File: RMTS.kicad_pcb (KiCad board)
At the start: 2 copper layers, 78.1 x 50.2 mm, 58 parts, among them J1 USB_B_Mini, J10 CONN_02, J2 Programmer, J3 Screw_Terminal_01x03, J4 Screw_Terminal_01x04, J5 Screw_Terminal_01x02, J6 Screw_Terminal_01x02, J7 Micro_SD_Card_Det_Hirose_DM3AT, J9 CONN_02, Q1 PMV20ENR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

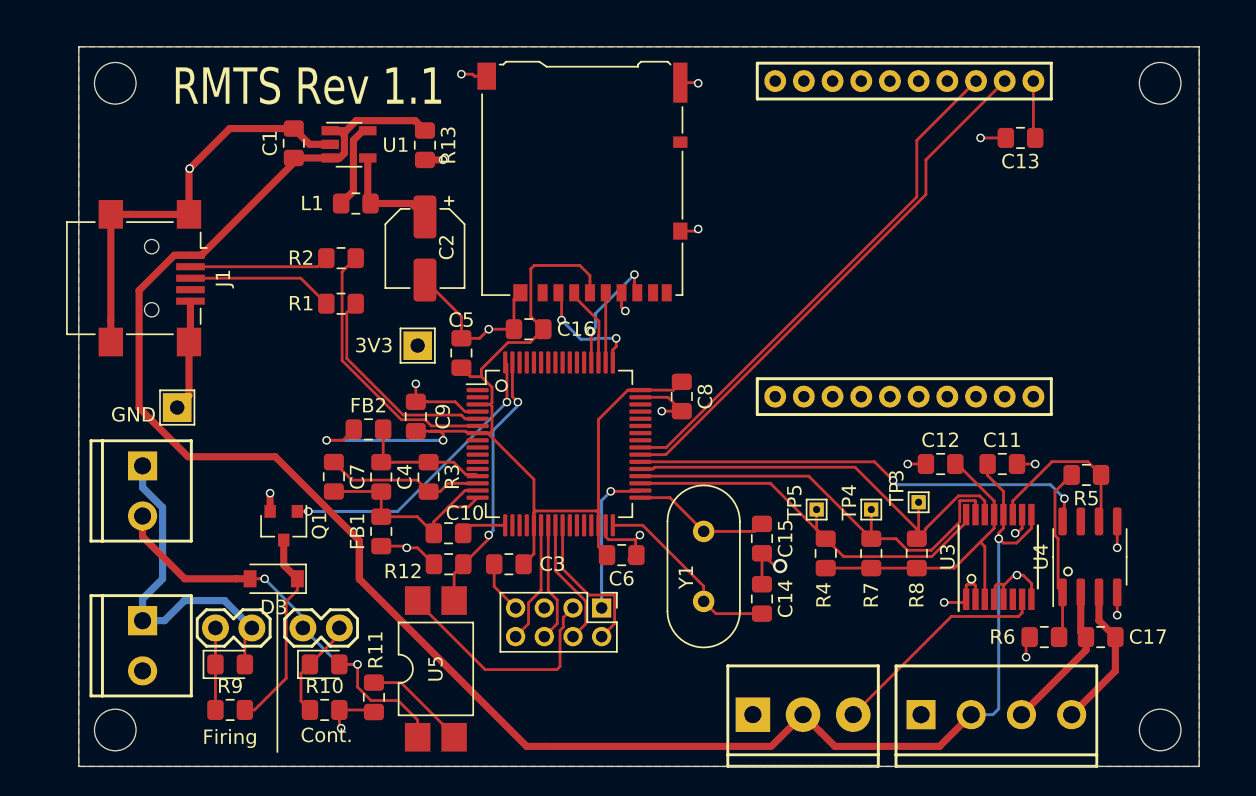
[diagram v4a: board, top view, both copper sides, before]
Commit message: Updated amplifier to MCP6N16, incremented revision number
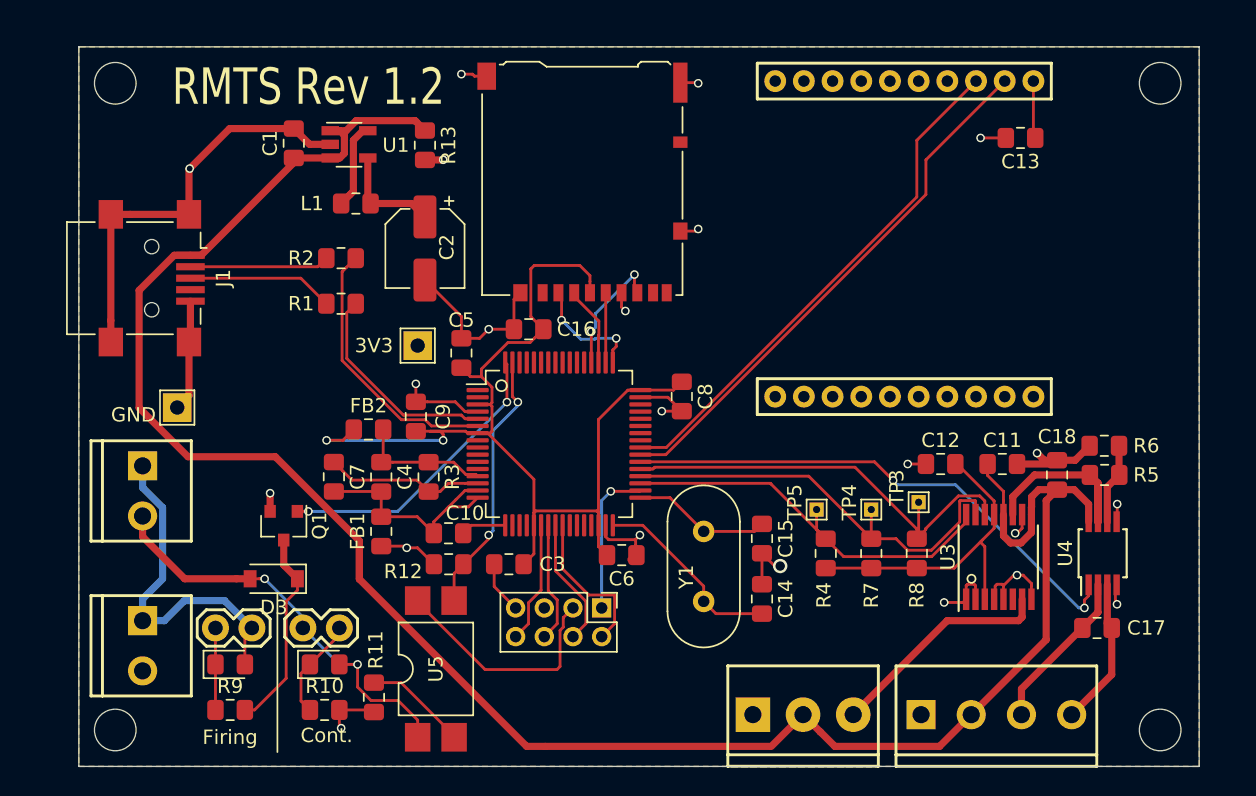
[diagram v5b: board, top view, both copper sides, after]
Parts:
- added C18: 0.1uF, Capacitor_SMD:C_0805_2012Metric_Pad1.15x1.40mm_HandSolder, F.Cu at (200.3, 92.1)
- U4: value MCP6N11 -> MCP6N16; footprint Package_SO:SOIC-8_3.9x4.9mm_P1.27mm -> Package_SO:MSOP-8_3x3mm_P0.65mm
- moved R6 14.0 mm to (203.6, 90.0)
- moved R5 1.27 mm to (203.6, 92.1), turned to 0 degrees
- moved U4 0.92 mm to (203.5, 97.5)
- moved C17 0.68 mm to (203.1, 102.7)
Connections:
- R5 pad 2: /FG0 -> Net-(R5-Pad2)
- R6 pad 1: /FG0 -> Net-(R5-Pad2)
- U4 pad 1: /FG0 -> /AMP_EN
- U4 pad 6: /LC0 -> Net-(R5-Pad2)
- U4 pad 7: +3V3 -> /LC0
- U4 pad 8: /AMP_EN -> /VBUS
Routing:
- net /FG0: track 12.1 -> 0.00 mm
- net /VBUS: track 134.4 -> 145.3 mm, vias 1 -> 0
- net Net-(R5-Pad2): track 0.00 -> 5.67 mm
- net /AMP_EN: track 32.3 -> 36.9 mm
- net GND: track 109.1 -> 113.2 mm, vias 23 -> 22
- net /LC0: track 11.9 -> 14.2 mm
- net Net-(C17-Pad2): track 10.5 -> 11.3 mm
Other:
- board text added: "RMTS Rev 1.2"
- board text removed: "RMTS Rev 1.1"

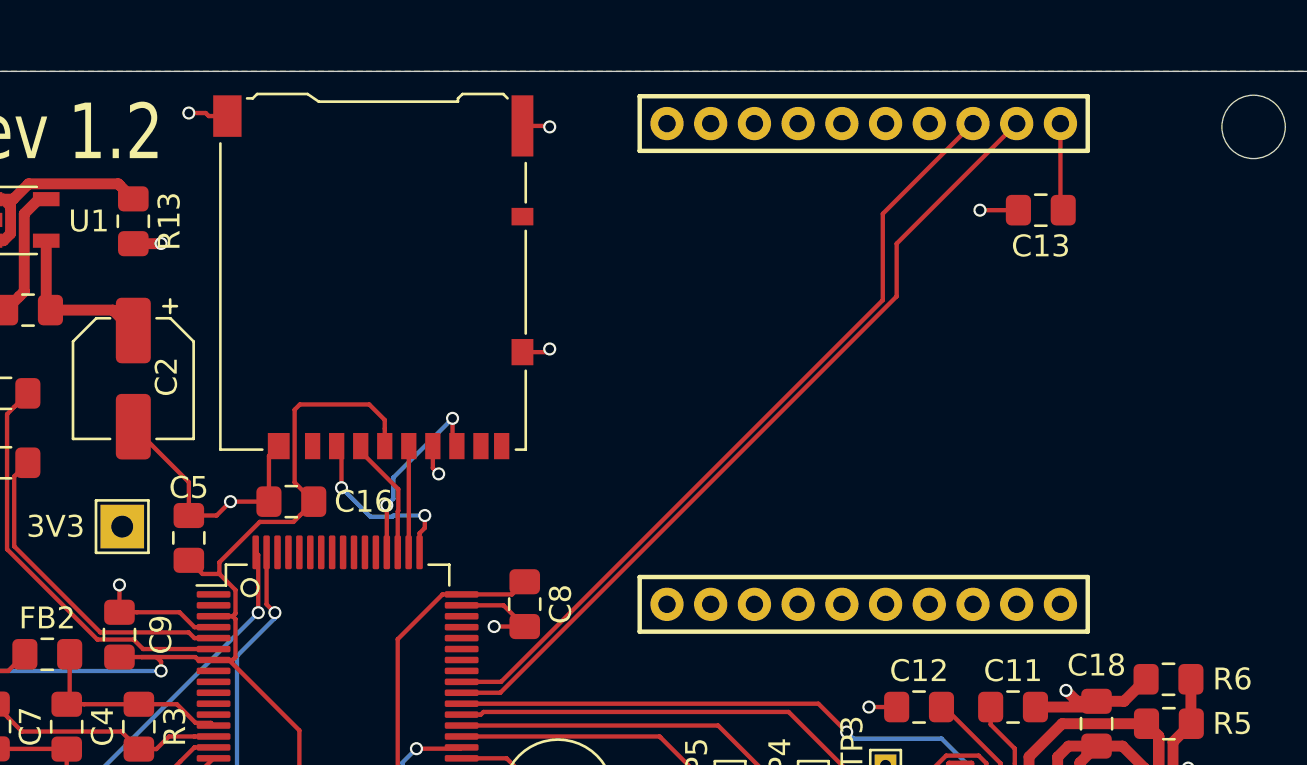
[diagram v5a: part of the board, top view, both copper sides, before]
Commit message: Flipped SD card, added external firing circuit
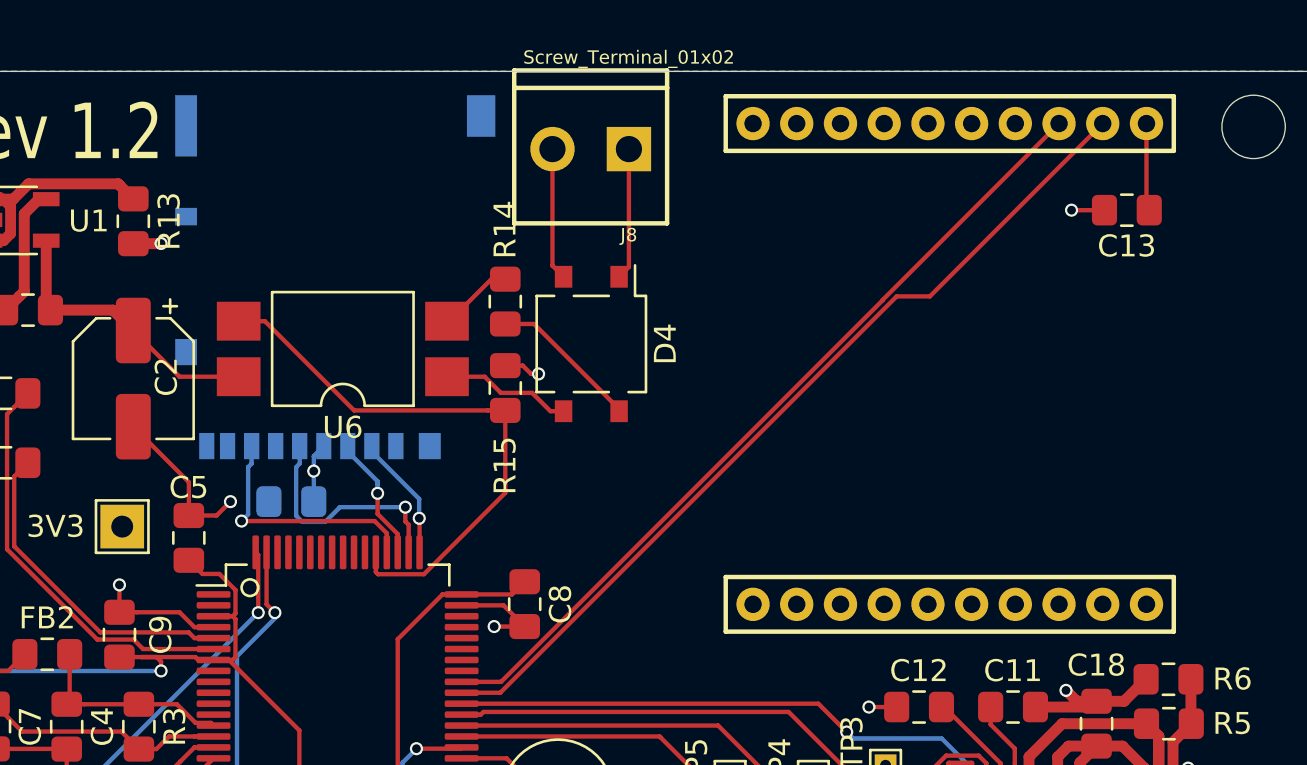
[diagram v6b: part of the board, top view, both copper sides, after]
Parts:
- added D4: MB4S, Package_TO_SOT_SMD:TO-269AA, F.Cu at (177.2, 74.7)
- added J8: Screw_Terminal_01x02, Connectors:SCREWTERMINAL-3.5MM-2, F.Cu at (178.9, 65.8)
- added R14: 500, Resistor_SMD:R_0805_2012Metric_Pad1.15x1.40mm_HandSolder, F.Cu at (173.2, 72.8)
- added R15: 500, Resistor_SMD:R_0805_2012Metric_Pad1.15x1.40mm_HandSolder, F.Cu at (173.2, 76.7)
- added U6: LTV-817S, Package_DIP:SMDIP-4_W9.53mm, F.Cu at (165.8, 74.9)
- C16, J7: moved to B.Cu
- moved C13 3.94 mm to (201.7, 68.6)
- moved JP1 3.94 mm to (182.6, 75.6)
- moved J7 1.74 mm to (165.4, 71.7), turned to 0 degrees
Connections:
- U2 pad 53: Net-(U2-Pad53) -> /EXT_FIRE
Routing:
- net /EXT_FIRE: track 0.00 -> 26.1 mm
- net GND: track 113.2 -> 104.3 mm, vias 22 -> 19
- net +3V3: track 123.8 -> 115.5 mm, vias 2 -> 3
- net Net-(D4-Pad4): track 0.00 -> 6.92 mm
- net Net-(D4-Pad2): track 0.00 -> 6.05 mm
- net Net-(D4-Pad1): track 0.00 -> 6.03 mm
- net Net-(D4-Pad3): track 0.00 -> 5.99 mm
- net /SD_CLK: track 4.86 -> 10.8 mm, vias 0 -> 1
- net Net-(R14-Pad1): track 0.00 -> 3.46 mm
- net /SD_DO: track 8.73 -> 11.4 mm, vias 2 -> 1
- net /DIN: track 37.6 -> 40.1 mm
- net /SD_CS: track 8.17 -> 5.76 mm, vias 2 -> 1
- net /DOUT: track 36.3 -> 37.9 mm
- net /SD_DI: track 5.58 -> 5.81 mm, vias 0 -> 1

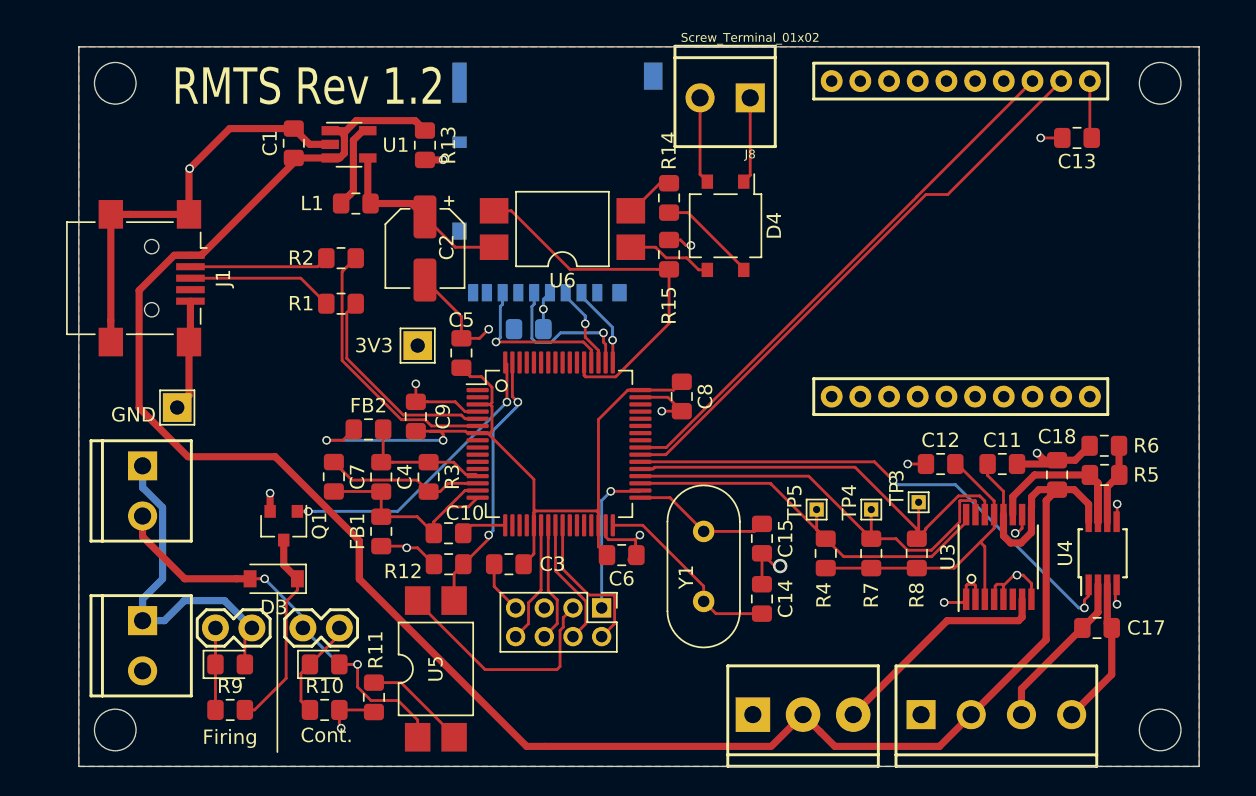
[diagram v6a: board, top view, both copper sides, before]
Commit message: Added power LED, moved labels, cleaned up some traces
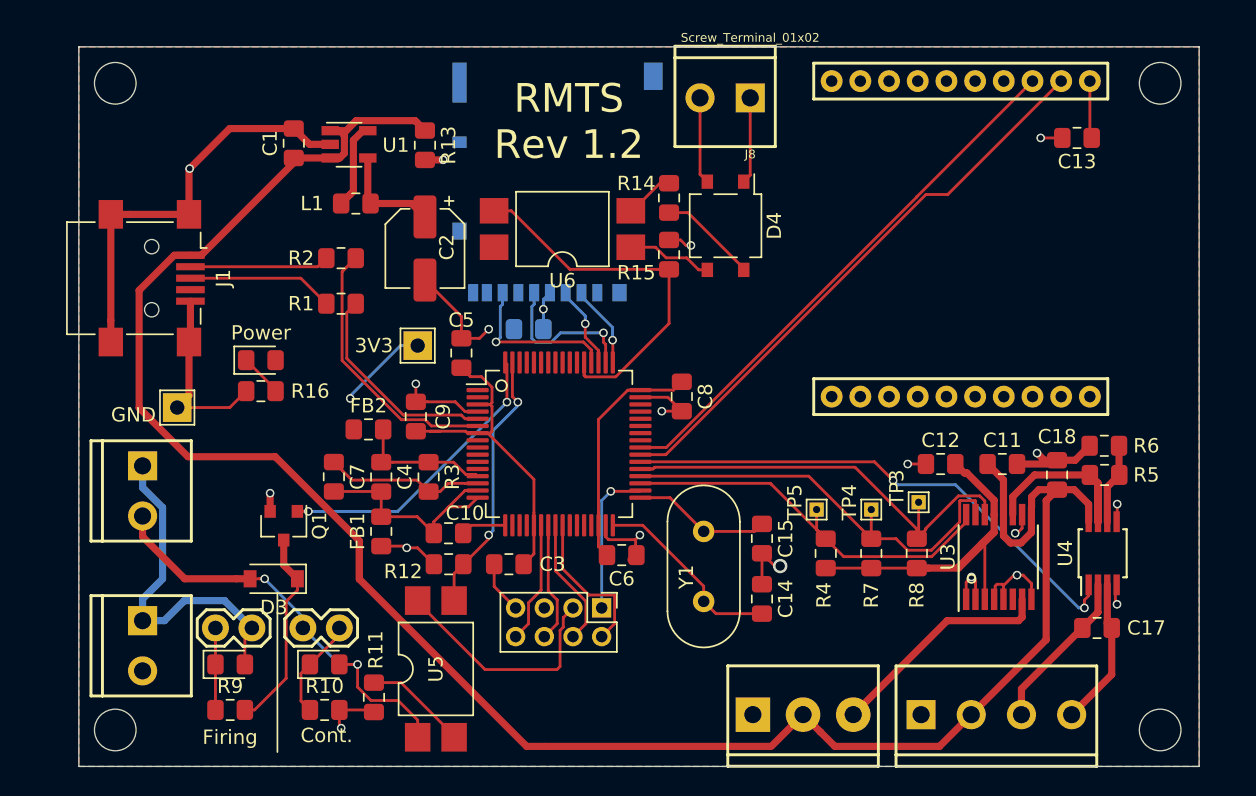
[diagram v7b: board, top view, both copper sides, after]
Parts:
- added D5: Power, LED_SMD:LED_0805_2012Metric_Pad1.15x1.40mm_HandSolder, F.Cu at (144.8, 84.1)
- added R16: 1k, Resistor_SMD:R_0805_2012Metric_Pad1.15x1.40mm_HandSolder, F.Cu at (144.8, 86.2)
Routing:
- net GND: track 104.3 -> 109.7 mm
- net Net-(D5-Pad1): track 0.00 -> 3.01 mm
- net +3V3: track 115.5 -> 112.9 mm, vias 3 -> 2
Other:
- board text added: "Power"
- board text added: "Trigger"

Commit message: Added status LED, hid labels
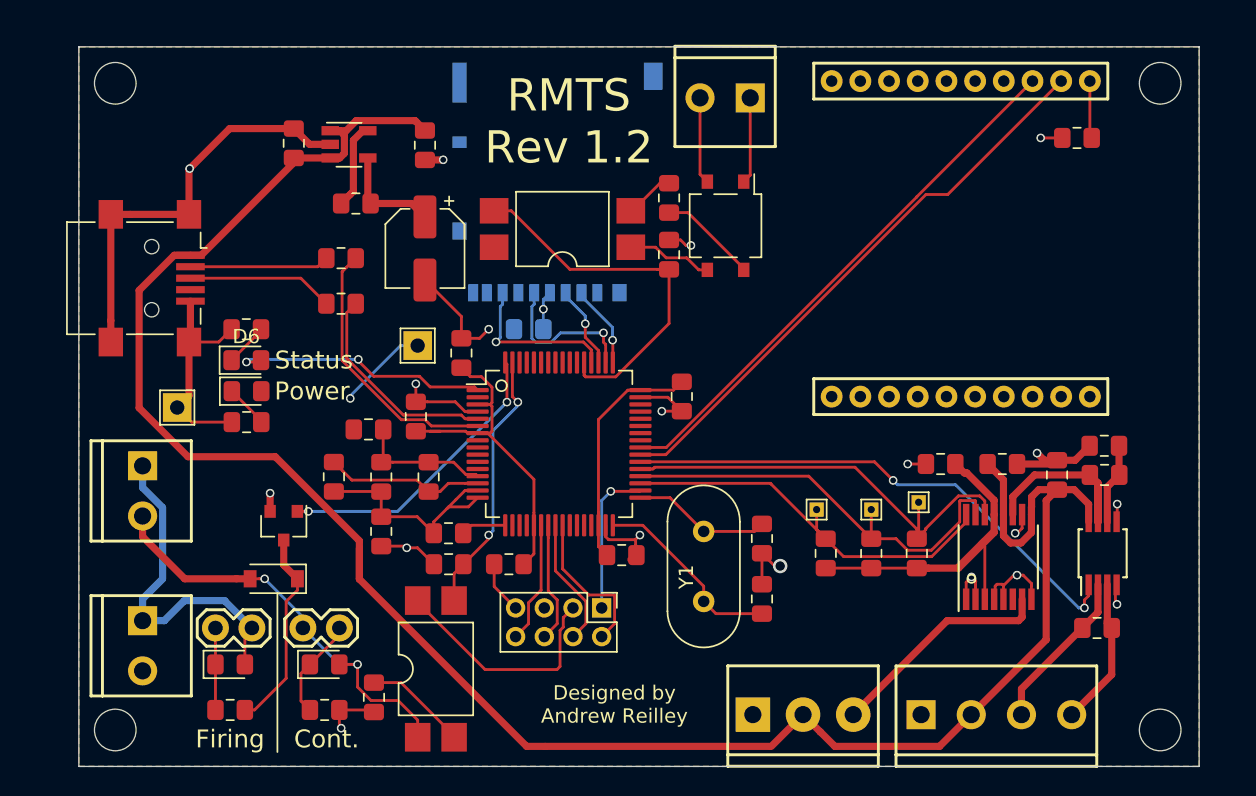
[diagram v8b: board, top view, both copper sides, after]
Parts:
- added D6: Status, LED_SMD:LED_0805_2012Metric_Pad1.15x1.40mm_HandSolder, F.Cu at (143.8, 84.1)
- added R17: 1k, Resistor_SMD:R_0805_2012Metric_Pad1.15x1.40mm_HandSolder, F.Cu at (143.8, 81.9)
- moved D5 2.38 mm to (143.8, 86.2)
- moved R16 2.38 mm to (143.8, 88.4)
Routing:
- net Net-(D6-Pad2): track 0.00 -> 18.3 mm, vias 0 -> 2
- net Net-(D6-Pad1): track 0.00 -> 3.01 mm
- net GND: track 109.7 -> 112.0 mm
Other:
- board text added: "Designed by Andrew Reilley"
- board text added: "Status"
